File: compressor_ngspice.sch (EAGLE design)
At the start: 49 parts, among them U1 MAX5419LETA+, U2 MAX5419LETA+, X1 OPAMP, X10 OPAMP, X3 OPAMP, X5 OPAMP, X6 OPAMP, X7 OPAMP, X8 OPAMP, X9 OPAMP

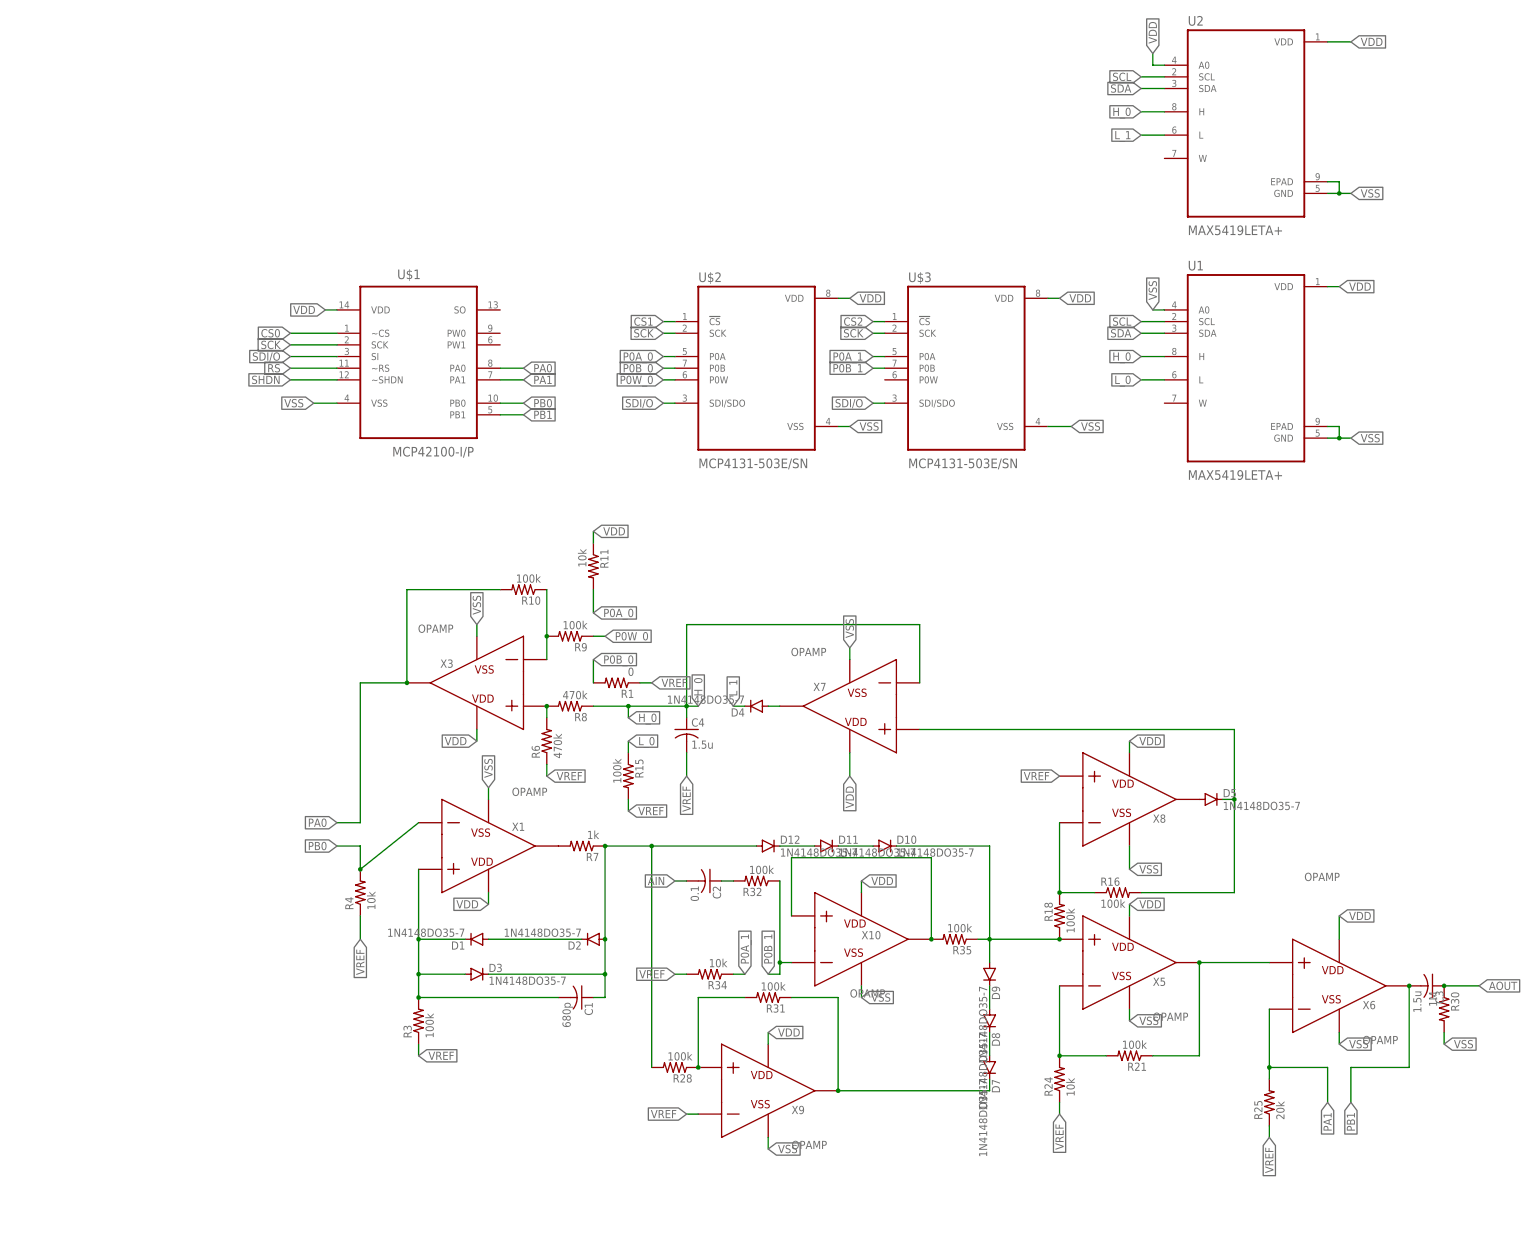
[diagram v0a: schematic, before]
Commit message: update, split out into schematics for each component
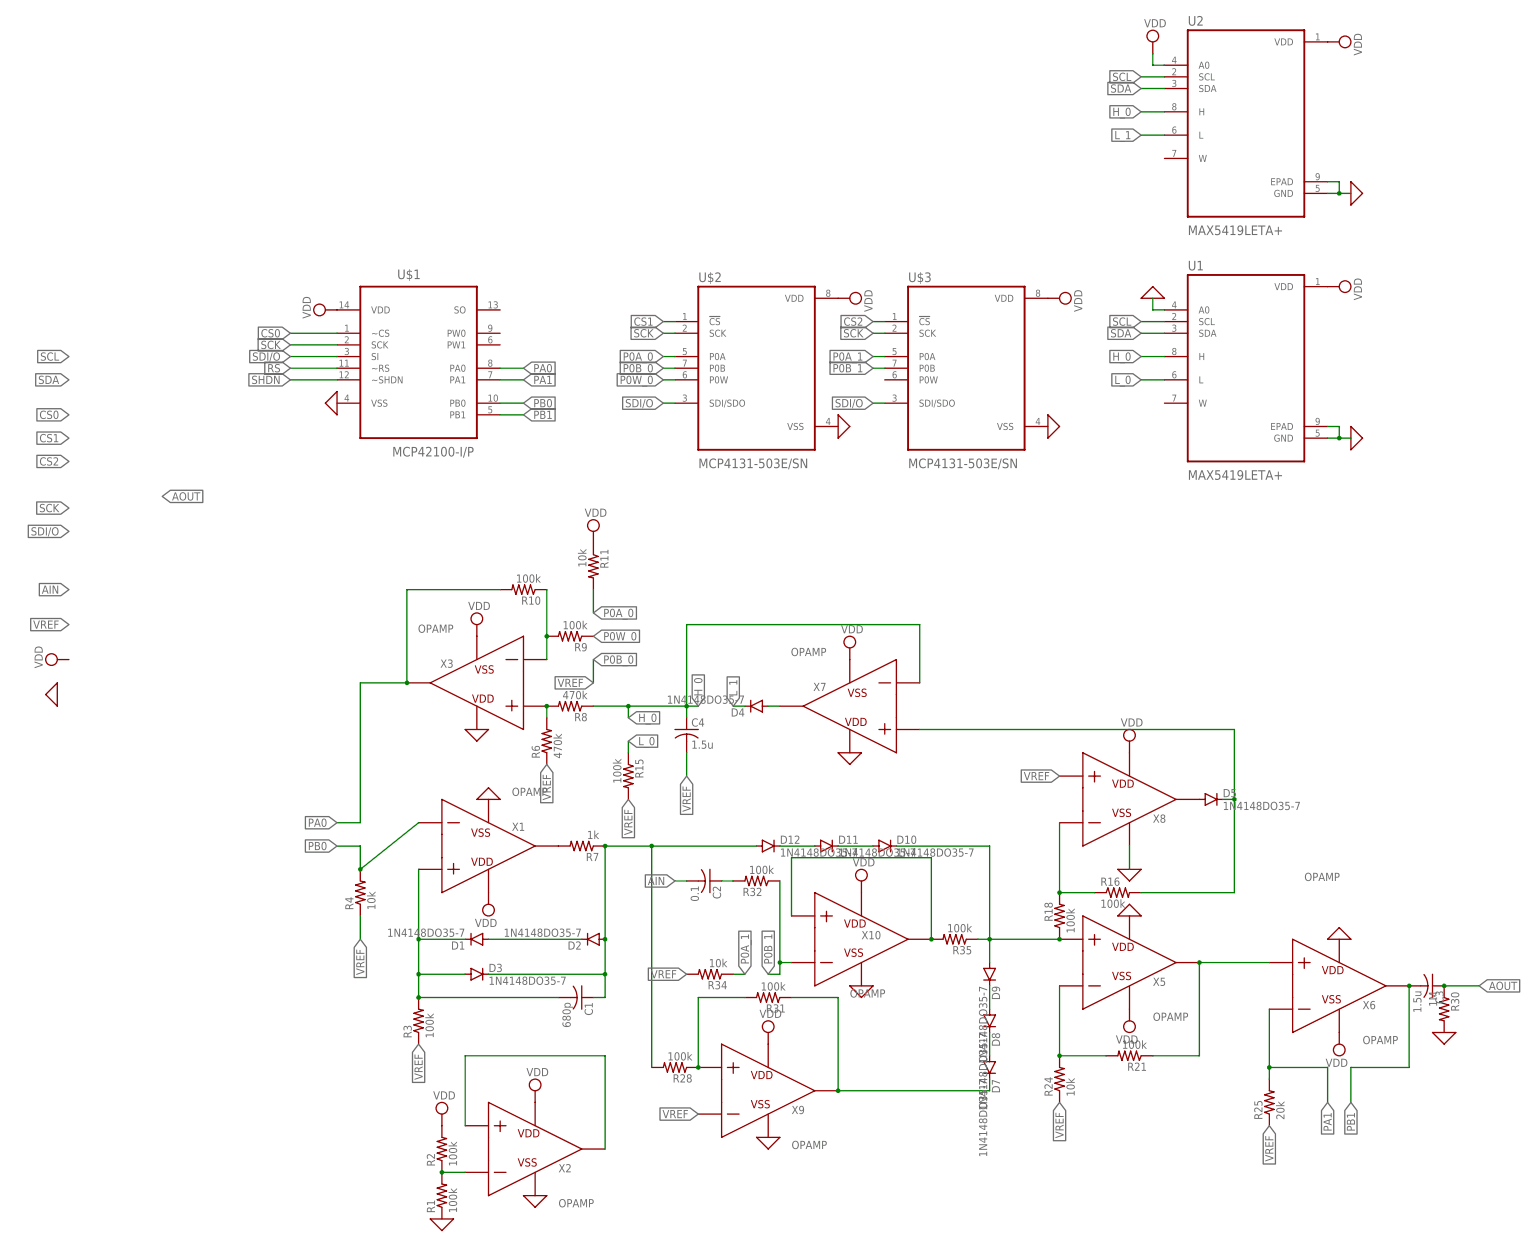
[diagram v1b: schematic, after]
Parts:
- added R2: 100k, rcl:R-US_0204/7
- added X2: OPAMP, ngspice-simulation:OPAMP
- R1: value 0 -> 100k
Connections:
- removed net VSS: R30.2, U$1.VSS, U$2.VSS, U$3.VSS, U1.A0, U1.EPAD, U1.GND, U2.EPAD, U2.GND, X1.VSS, X10.VSS, X3.VSS, X5.VSS, X6.VSS, X7.VSS, X8.VSS, X9.VSS
- new net 0: R1.1, R30.2, U$1.VSS, U$2.VSS, U$3.VSS, U1.A0, U1.EPAD, U1.GND, U2.EPAD, U2.GND, X1.VSS, X10.VSS, X2.VSS, X3.VDD, X5.VDD, X6.VDD, X7.VDD, X8.VSS, X9.VSS
- new net N$10: R11.2
- new net N$11: C4.2
- new net N$4: R1.2, R2.1, X2.N
- new net N$5: X2.P, X2.VOUT
- net P0A_0: no longer R11.2
- net P0B_0: no longer R1.2
- net P0W_0: no longer R9.1
- net VDD: now also R2.2, X2.VDD, X3.VSS, X5.VSS, X6.VSS, X7.VSS; no longer X3.VDD, X5.VDD, X6.VDD, X7.VDD
- net VREF: no longer C4.2, R1.1, R15.2, R24.1, R25.1, R3.1, R34.2, R6.1, X9.N
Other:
- moved on the sheet: R1
